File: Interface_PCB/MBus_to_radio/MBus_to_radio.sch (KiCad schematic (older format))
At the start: 21 parts, among them Q1 BC847, Q2 BC857, U1 AP63205WU-7, X1 TB003-500-P02BE

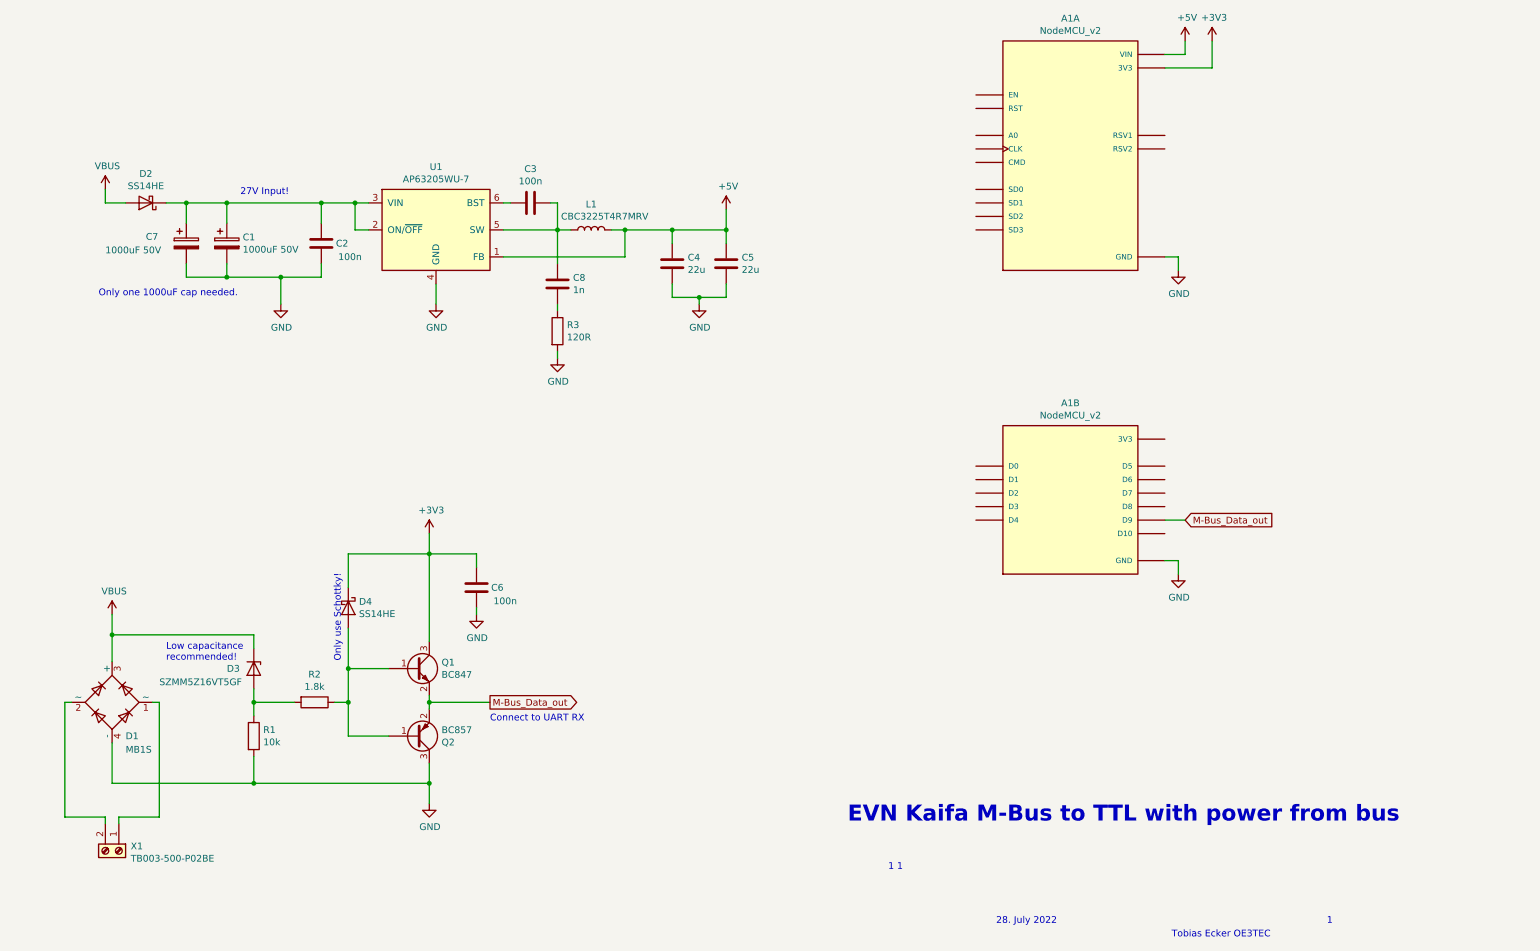
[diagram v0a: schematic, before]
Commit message: update PCB V2 to version that was produced
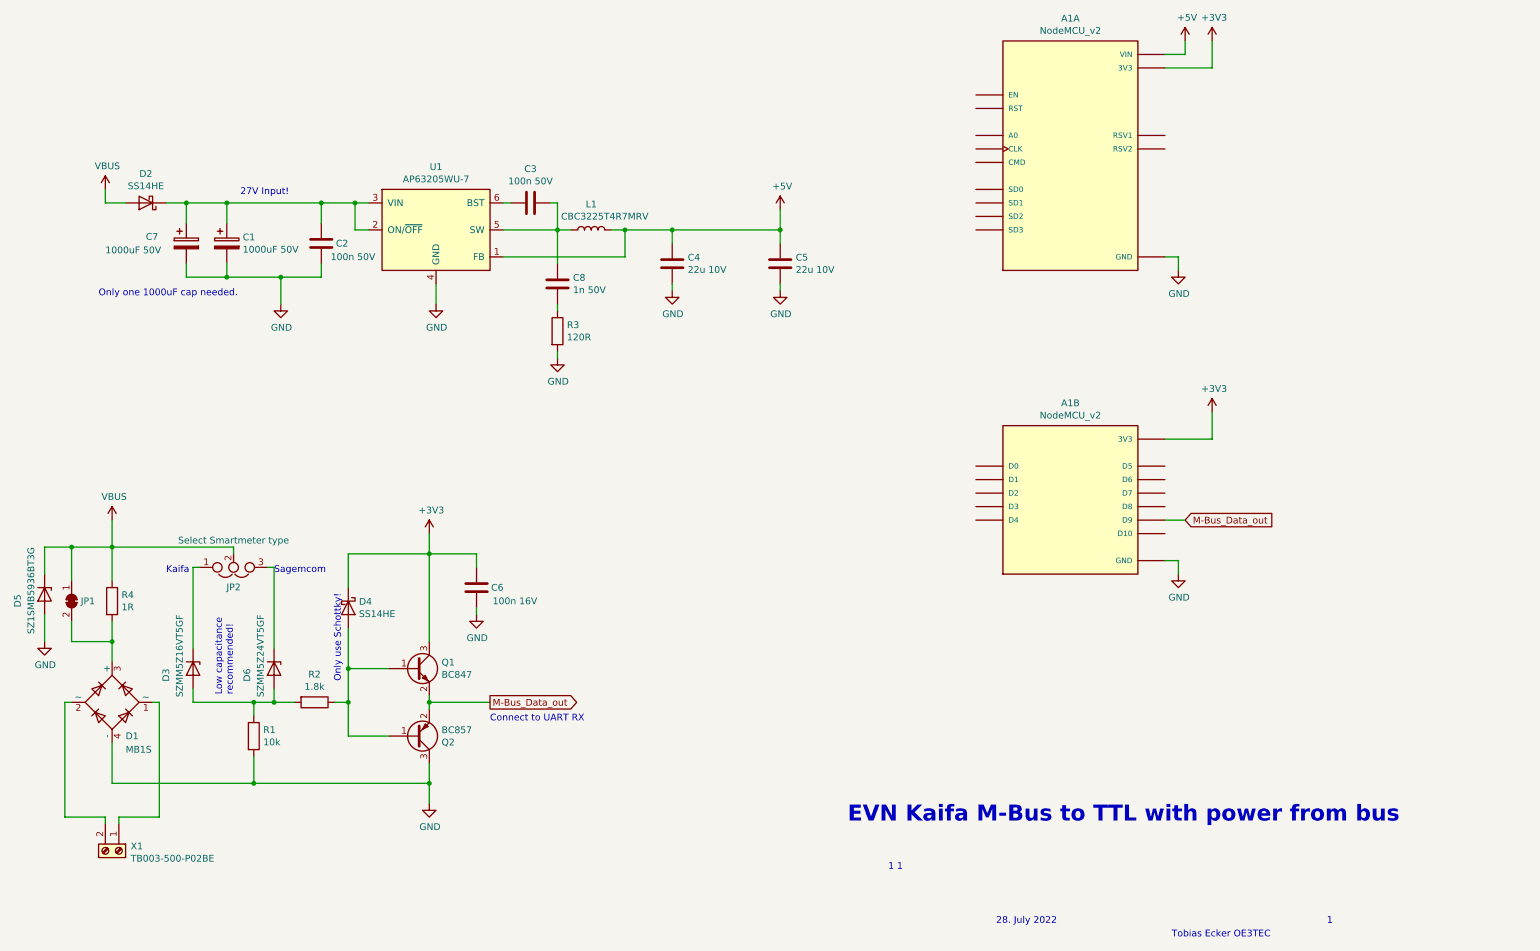
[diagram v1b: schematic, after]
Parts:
- added D5: SZ1SMB5936BT3G, Diode_SMD:D_SMB-SMC_Universal_Handsoldering, symbol Device:D_Zener
- added D6: SZMM5Z24VT5GF, Diode_SMD:D_SOD-523, symbol Device:D_Zener
- added JP1: SolderJumper_2_Bridged, Jumper:SolderJumper-2_P1.3mm_Bridged_RoundedPad1.0x1.5mm, symbol Jumper:SolderJumper_2_Bridged
- added JP2: Select Smartmeter type, Connector_PinHeader_2.54mm:PinHeader_1x03_P2.54mm_Vertical, symbol Device:Jumper_NC_Dual
- added R4: 1R, Resistor_SMD:R_1812_4532Metric, symbol Device:R
- C2, C3: value 100n -> 100n 50V
- C4, C5: value 22u -> 22u 10V
- C6: value 100n -> 100n 16V
- C8: value 1n -> 1n 50V
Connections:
- net +3V3: now also A1.J2_15 (3V3), A1.J2_6 (3V3)
- net GND: now also D5.2 (A)
- net VBUS: now also D5.1 (K), JP1.1 (A), JP2.2, R4.1; no longer D1.3 (+), D3.1 (K)
- net at D3.2 (A), R1.1, R2.2: now also D6.2 (A)
- new net: D1.3 (+), JP1.2 (B), R4.2
- new net: D3.1 (K), JP2.1
- new net: D6.1 (K), JP2.3
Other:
- note added: "Kaifa"
- note added: "Sagemcom"
- moved on the sheet: C5, D3
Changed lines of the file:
@@
 L Device:D_Zener D3
 U 1 1 62E1D62F
-P 2600 5750
-F 0 "D3" V 2600 5550 50  0000 L CNN
-F 1 "SZMM5Z16VT5GF" V 2700 5050 50  0000 L CNN
-F 2 "Diode_SMD:D_SOD-523" H 2600 5750 50  0001 C CNN
-F 3 "~" H 2600 5750 50  0001 C CNN
-	1    2600 5750
+P 2150 5750
+F 0 "D3" H 2150 5550 50  0000 L CNN
+F 1 "SZMM5Z16VT5GF" H 1750 5650 50  0000 L CNN
+F 2 "Diode_SMD:D_SOD-523" H 2150 5750 50  0001 C CNN
+F 3 "~" H 2150 5750 50  0001 C CNN
+	1    2150 5750
 	0    1    1    0
 $EndComp
@@
 	2600 6600 3900 6600
 Wire Wire Line
-	2600 5900 2600 6000
-Wire Wire Line
-	2900 6000 2600 6000
-Connection ~ 2600 6000
+	2900 6000 2750 6000
 Wire Wire Line
 	2600 6000 2600 6100
@@
 Connection ~ 3300 6000
 Connection ~ 3300 5750
-Wire Wire Line
-	1550 5700 1550 5500
-Wire Wire Line
-	1550 5500 2600 5500
-Wire Wire Line
-	2600 5500 2600 5600
 $Comp
 L Device:D_Schottky D2
@@
 Text Notes 9400 7750 0    50   ~ 0
 Tobias Ecker OE3TEC
-Text Notes 3250 5700 1    50   ~ 0
+Text Notes 3250 5850 1    50   ~ 0
 Only use Schottky!
-Text Notes 1950 5700 0    50   ~ 0
+Text Notes 2450 5950 1    50   ~ 0
 Low capacitance\nrecommended!
 Text Notes 4350 6150 0    50   ~ 0
@@
 P 4650 2300
 F 0 "C3" V 4902 2300 50  0000 C CNN
-F 1 "100n" V 4811 2300 50  0000 C CNN
+F 1 "100n 50V" V 4811 2300 50  0000 C CNN
 F 2 "Capacitor_SMD:C_0603_1608Metric" H 4688 2150 50  0001 C CNN
 F 3 "~" H 4650 2300 50  0001 C CNN
@@
 P 5700 2750
 F 0 "C4" H 5585 2704 50  0000 R CNN
-F 1 "22u" H 5585 2795 50  0000 R CNN
+F 1 "22u 10V" H 5585 2795 50  0000 R CNN
 F 2 "Capacitor_SMD:C_1206_3216Metric" H 5738 2600 50  0001 C CNN
 F 3 "~" H 5700 2750 50  0001 C CNN
@@
 L Device:C C5
 U 1 1 6357B689
-P 6100 2750
-F 0 "C5" H 5985 2704 50  0000 R CNN
-F 1 "22u" H 5985 2795 50  0000 R CNN
-F 2 "Capacitor_SMD:C_1206_3216Metric" H 6138 2600 50  0001 C CNN
-F 3 "~" H 6100 2750 50  0001 C CNN
-	1    6100 2750
+P 6500 2750
+F 0 "C5" H 6385 2704 50  0000 R CNN
+F 1 "22u 10V" H 6385 2795 50  0000 R CNN
+F 2 "Capacitor_SMD:C_1206_3216Metric" H 6538 2600 50  0001 C CNN
+F 3 "~" H 6500 2750 50  0001 C CNN
+	1    6500 2750
 	-1   0    0    1
 $EndComp
@@
 	5350 2500 5700 2500
 Wire Wire Line
-	6100 2500 6100 2600
+	6500 2500 6500 2600
 Connection ~ 5350 2500
 Wire Wire Line
 	5700 2600 5700 2500
-Connection ~ 5700 2500
-Wire Wire Line
-	5700 2500 6100 2500
-Wire Wire Line
-	6100 2900 6100 3000
-Wire Wire Line
-	6100 3000 5900 3000
-Wire Wire Line
-	5700 2900 5700 3000
 $Comp
 L power:GND #PWR05
@@
 	1    0    0    -1
 $EndComp
-$Comp
-L power:GND #PWR07
-U 1 1 63583FF5
-P 5900 3050
-F 0 "#PWR07" H 5900 2800 50  0001 C CNN
-F 1 "GND" H 5905 2877 50  0000 C CNN
-F 2 "" H 5900 3050 50  0001 C CNN
-F 3 "" H 5900 3050 50  0001 C CNN
-	1    5900 3050
-	1    0    0    -1
-$EndComp
-Wire Wire Line
-	5900 3050 5900 3000
-Connection ~ 5900 3000
-Wire Wire Line
-	5900 3000 5700 3000
 Wire Wire Line
 	3950 2900 3950 3050
@@
 P 3100 2600
 F 0 "C2" H 2900 2600 50  0000 L CNN
-F 1 "100n" H 2800 2700 50  0000 L CNN
+F 1 "100n 50V" H 2700 2700 50  0000 L CNN
 F 2 "Capacitor_SMD:C_0603_1608Metric" H 3138 2450 50  0001 C CNN
 F 3 "~" H 3100 2600 50  0001 C CNN
@@
 L power:+5V #PWR08
 U 1 1 635B5703
-P 6100 2350
-F 0 "#PWR08" H 6100 2200 50  0001 C CNN
-F 1 "+5V" H 6115 2523 50  0000 C CNN
-F 2 "" H 6100 2350 50  0001 C CNN
-F 3 "" H 6100 2350 50  0001 C CNN
-	1    6100 2350
-	1    0    0    -1
-$EndComp
-Wire Wire Line
-	6100 2350 6100 2500
-Connection ~ 6100 2500
+P 6500 2350
+F 0 "#PWR08" H 6500 2200 50  0001 C CNN
+F 1 "+5V" H 6515 2523 50  0000 C CNN
+F 2 "" H 6500 2350 50  0001 C CNN
+F 3 "" H 6500 2350 50  0001 C CNN
+	1    6500 2350
+	1    0    0    -1
+$EndComp
+Wire Wire Line
+	6500 2350 6500 2500
+Connection ~ 6500 2500
 $Comp
 L power:VBUS #PWR02
@@
 L power:VBUS #PWR04
 U 1 1 635BD71F
-P 1550 5350
-F 0 "#PWR04" H 1550 5200 50  0001 C CNN
-F 1 "VBUS" H 1565 5523 50  0000 C CNN
-F 2 "" H 1550 5350 50  0001 C CNN
-F 3 "" H 1550 5350 50  0001 C CNN
-	1    1550 5350
-	1    0    0    -1
-$EndComp
-Wire Wire Line
-	1550 5350 1550 5500
-Connection ~ 1550 5500
+P 1550 4650
+F 0 "#PWR04" H 1550 4500 50  0001 C CNN
+F 1 "VBUS" H 1565 4823 50  0000 C CNN
+F 2 "" H 1550 4650 50  0001 C CNN
+F 3 "" H 1550 4650 50  0001 C CNN
+	1    1550 4650
+	1    0    0    -1
+$EndComp
 $Comp
 L M_bus_radio:NodeMCU_v2 A1
@@
 P 4250 5150
 F 0 "C6" H 4050 5150 50  0000 L CNN
-F 1 "100n" H 3950 5250 50  0000 L CNN
+F 1 "100n 16V" H 3800 5250 50  0000 L CNN
 F 2 "Capacitor_SMD:C_0603_1608Metric" H 4288 5000 50  0001 C CNN
 F 3 "~" H 4250 5150 50  0001 C CNN
@@
 P 4850 2900
 F 0 "C8" H 4735 2854 50  0000 R CNN
-F 1 "1n" H 4735 2945 50  0000 R CNN
+F 1 "1n 50V" H 4735 2945 50  0000 R CNN
 F 2 "Capacitor_SMD:C_0603_1608Metric" H 4888 2750 50  0001 C CNN
 F 3 "~" H 4850 2900 50  0001 C CNN
@@
 Wire Wire Line
 	4850 3450 4850 3400
+$Comp
+L power:+3V3 #PWR017
+U 1 1 63711545
+P 9700 3850
+F 0 "#PWR017" H 9700 3700 50  0001 C CNN
+F 1 "+3V3" H 9715 4023 50  0000 C CNN
+F 2 "" H 9700 3850 50  0001 C CNN
+F 3 "" H 9700 3850 50  0001 C CNN
+	1    9700 3850
+	1    0    0    -1
+$EndComp
+Wire Wire Line
+	9350 4050 9700 4050
+Wire Wire Line
+	9700 4050 9700 3850
+$Comp
+L Device:Jumper_NC_Dual JP2
+U 1 1 6386E88C
+P 2450 5000
+F 0 "JP2" H 2450 5147 50  0000 C CNN
+F 1 "Select Smartmeter type" H 2450 4800 50  0000 C CNN
+F 2 "Connector_PinHeader_2.54mm:PinHeader_1x03_P2.54mm_Vertical" H 2450 5000 50  0001 C CNN
+F 3 "~" H 2450 5000 50  0001 C CNN
+	1    2450 5000
+	1    0    0    1
+$EndComp
+$Comp
+L Device:D_Zener D6
+U 1 1 63877958
+P 2750 5750
+F 0 "D6" H 2750 5550 50  0000 L CNN
+F 1 "SZMM5Z24VT5GF" H 2350 5650 50  0000 L CNN
+F 2 "Diode_SMD:D_SOD-523" H 2750 5750 50  0001 C CNN
+F 3 "~" H 2750 5750 50  0001 C CNN
+	1    2750 5750
+	0    1    1    0
+$EndComp
+Wire Wire Line
+	2150 6000 2150 5900
+Connection ~ 2600 6000
+Wire Wire Line
+	2150 6000 2600 6000
+Wire Wire Line
+	2150 5600 2150 5000
+Wire Wire Line
+	2150 5000 2200 5000
+Wire Wire Line
+	2700 5000 2750 5000
+Wire Wire Line
+	2750 5000 2750 5600
+Wire Wire Line
+	2750 5900 2750 6000
+Connection ~ 2750 6000
+Wire Wire Line
+	2750 6000 2600 6000
+Wire Wire Line
+	2450 4900 2450 4850
+Wire Wire Line
+	2450 4850 1550 4850
+Wire Wire Line
+	1550 4850 1550 4650
+Text Notes 1950 5050 0    50   ~ 0
+Kaifa
+Text Notes 2750 5050 0    50   ~ 0
+Sagemcom
+Wire Wire Line
+	5700 2500 6500 2500
+Connection ~ 5700 2500
+$Comp
+L power:GND #PWR015
+U 1 1 638BF2E2
+P 5700 2950
+F 0 "#PWR015" H 5700 2700 50  0001 C CNN
+F 1 "GND" H 5705 2777 50  0000 C CNN
+F 2 "" H 5700 2950 50  0001 C CNN
+F 3 "" H 5700 2950 50  0001 C CNN
+	1    5700 2950
+	1    0    0    -1
+$EndComp
+$Comp
+L power:GND #PWR016
+U 1 1 638BF606
+P 6500 2950
+F 0 "#PWR016" H 6500 2700 50  0001 C CNN
+F 1 "GND" H 6505 2777 50  0000 C CNN
+F 2 "" H 6500 2950 50  0001 C CNN
+F 3 "" H 6500 2950 50  0001 C CNN
+	1    6500 2950
+	1    0    0    -1
+$EndComp
+Wire Wire Line
+	5700 2900 5700 2950
+Wire Wire Line
+	6500 2900 6500 2950
+$Comp
+L Device:D_Zener D5
+U 1 1 638CC343
+P 1050 5200
+F 0 "D5" H 1050 5000 50  0000 L CNN
+F 1 "SZ1SMB5936BT3G" H 700 5100 50  0000 L CNN
+F 2 "Diode_SMD:D_SMB-SMC_Universal_Handsoldering" H 1050 5200 50  0001 C CNN
+F 3 "~" H 1050 5200 50  0001 C CNN
+	1    1050 5200
+	0    1    1    0
+$EndComp
+$Comp
+L Device:R R4
+U 1 1 638CD487
+P 1550 5250
+F 0 "R4" H 1620 5296 50  0000 L CNN
+F 1 "1R" H 1620 5205 50  0000 L CNN
+F 2 "Resistor_SMD:R_1812_4532Metric" V 1480 5250 50  0001 C CNN
+F 3 "~" H 1550 5250 50  0001 C CNN
+	1    1550 5250
+	1    0    0    -1
+$EndComp
+Wire Wire Line
+	1550 5100 1550 4850
+Connection ~ 1550 4850
+Wire Wire Line
+	1550 5400 1550 5550
+$Comp
+L Jumper:SolderJumper_2_Bridged JP1
+U 1 1 638D526F
+P 1250 5250
+F 0 "JP1" V 1250 5318 50  0000 L CNN
+F 1 "SolderJumper_2_Bridged" V 1295 5318 50  0001 L CNN
+F 2 "Jumper:SolderJumper-2_P1.3mm_Bridged_RoundedPad1.0x1.5mm" H 1250 5250 50  0001 C CNN
+F 3 "~" H 1250 5250 50  0001 C CNN
+	1    1250 5250
+	0    1    1    0
+$EndComp
+Wire Wire Line
+	1250 5100 1250 4850
+Wire Wire Line
+	1250 4850 1550 4850
+Wire Wire Line
+	1550 5550 1250 5550
+Wire Wire Line
+	1250 5550 1250 5400
+Connection ~ 1550 5550
+Wire Wire Line
+	1550 5550 1550 5700
+Wire Wire Line
+	1050 4850 1250 4850
+Wire Wire Line
+	1050 4850 1050 5050
+Connection ~ 1250 4850
+$Comp
+L power:GND #PWR07
+U 1 1 638E0353
+P 1050 5550
+F 0 "#PWR07" H 1050 5300 50  0001 C CNN
+F 1 "GND" H 1055 5377 50  0000 C CNN
+F 2 "" H 1050 5550 50  0001 C CNN
+F 3 "" H 1050 5550 50  0001 C CNN
+	1    1050 5550
+	1    0    0    -1
+$EndComp
+Wire Wire Line
+	1050 5350 1050 5550
 $EndSCHEMATC

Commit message: clear up HW dir
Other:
- note added: "2"
- note added: "2nd January 2023"
- note removed: "1"
- note removed: "28. July 2022"
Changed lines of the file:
@@
 1 1
 Text Notes 8100 7650 0    50   ~ 0
-28. July 2022
+2nd January 2023
 Text Notes 10550 7650 0    50   ~ 0
-1
+2
 Text Notes 9400 7750 0    50   ~ 0
 Tobias Ecker OE3TEC
